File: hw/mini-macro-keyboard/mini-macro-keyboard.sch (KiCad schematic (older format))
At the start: 17 parts

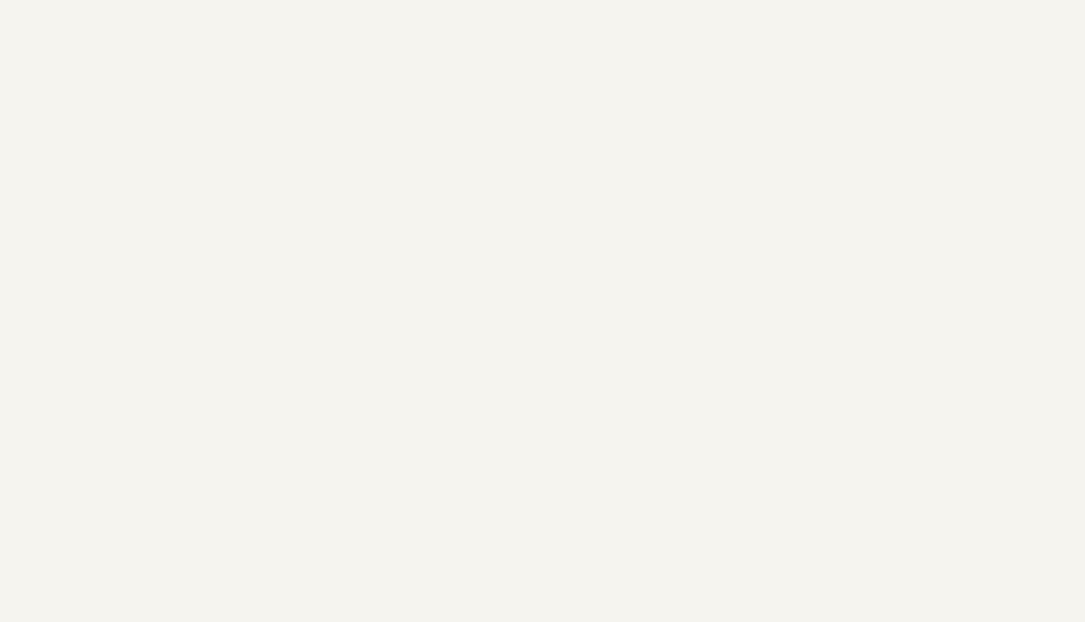
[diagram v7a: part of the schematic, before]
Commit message: feat(hw): add buck dc/dc converter to the schematic
Signed-off-by: Ivan Kovalenko <s1ckretbox@gmail.com>
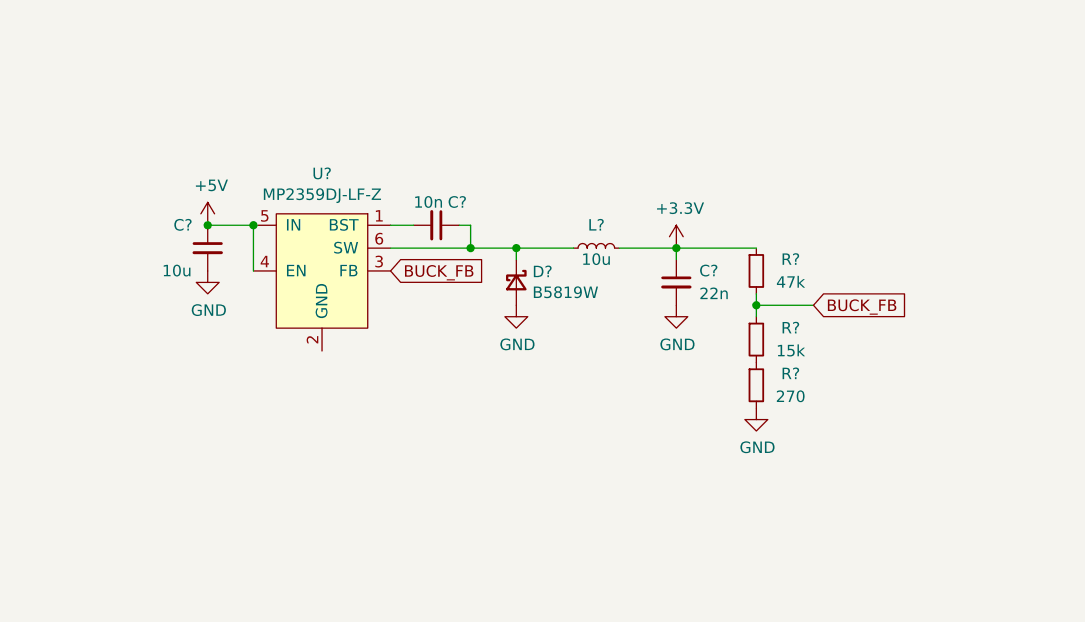
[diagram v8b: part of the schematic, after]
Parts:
- added C?: 10u, symbol Device:C_Small
- added C?: 10n, symbol Device:C_Small
- added C?: 22n, symbol Device:C_Small
- added D?: B5819W, symbol Device:D_Schottky_Small
- added L?: 10u, symbol Device:L_Small
- added R?: 47k, symbol Device:R_Small
- added R?: 15k, symbol Device:R_Small
- added R?: 270, symbol Device:R_Small
- added U?: MP2359DJ-LF-Z, symbol mini-macro-keyboard:MP2359DJ-LF-Z
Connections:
- net +3V3: now also C?.1, L?.2, R?.1
- net +5V: now also C?.1, U?.4 (EN), U?.5 (IN)
- net GND: now also C?.2, C?.2, D?.2 (A), R?.2
- new net: C?.2, U?.1 (BST)
- new net: C?.1, D?.1 (K), L?.1, U?.6 (SW)
- new net: R?.1, R?.2
- new net BUCK_FB: R?.1, R?.2, U?.3 (FB)
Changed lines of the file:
@@
 Text GLabel 7500 1100 2    50   Input ~ 0
 USB_D-
+$Comp
+L mini-macro-keyboard:MP2359DJ-LF-Z U?
+U 1 1 6003F08A
+P 4000 3000
+F 0 "U?" H 4000 3375 50  0000 C CNN
+F 1 "MP2359DJ-LF-Z" H 4000 3284 50  0000 C CNN
+F 2 "" H 4000 3000 50  0001 C CNN
+F 3 "" H 4000 3000 50  0001 C CNN
+	1    4000 3000
+	1    0    0    -1
+$EndComp
+$Comp
+L power:+5V #PWR?
+U 1 1 6003FF31
+P 3500 2850
+F 0 "#PWR?" H 3500 2700 50  0001 C CNN
+F 1 "+5V" H 3515 3023 50  0000 C CNN
+F 2 "" H 3500 2850 50  0001 C CNN
+F 3 "" H 3500 2850 50  0001 C CNN
+	1    3500 2850
+	1    0    0    -1
+$EndComp
+$Comp
+L power:GND #PWR?
+U 1 1 60040921
+P 3500 3050
+F 0 "#PWR?" H 3500 2800 50  0001 C CNN
+F 1 "GND" H 3505 2877 50  0000 C CNN
+F 2 "" H 3500 3050 50  0001 C CNN
+F 3 "" H 3500 3050 50  0001 C CNN
+	1    3500 3050
+	1    0    0    -1
+$EndComp
+$Comp
+L Device:C_Small C?
+U 1 1 600410FF
+P 3500 2950
+F 0 "C?" H 3350 3050 50  0000 L CNN
+F 1 "10u" H 3300 2850 50  0000 L CNN
+F 2 "" H 3500 2950 50  0001 C CNN
+F 3 "~" H 3500 2950 50  0001 C CNN
+	1    3500 2950
+	1    0    0    -1
+$EndComp
+Wire Wire Line
+	3700 2850 3700 3050
+Wire Wire Line
+	3700 2850 3500 2850
+Connection ~ 3700 2850
+Connection ~ 3500 2850
+$Comp
+L Device:D_Schottky_Small D?
+U 1 1 600485AC
+P 4850 3100
+F 0 "D?" V 4804 3170 50  0000 L CNN
+F 1 "B5819W" V 4895 3170 50  0000 L CNN
+F 2 "" V 4850 3100 50  0001 C CNN
+F 3 "~" V 4850 3100 50  0001 C CNN
+	1    4850 3100
+	0    1    1    0
+$EndComp
+$Comp
+L Device:C_Small C?
+U 1 1 600491AA
+P 4500 2850
+F 0 "C?" V 4400 2900 50  0000 L CNN
+F 1 "10n" V 4400 2750 50  0000 L CNN
+F 2 "" H 4500 2850 50  0001 C CNN
+F 3 "~" H 4500 2850 50  0001 C CNN
+	1    4500 2850
+	0    1    1    0
+$EndComp
+Wire Wire Line
+	4300 2850 4400 2850
+$Comp
+L Device:L_Small L?
+U 1 1 6004E9B3
+P 5200 2950
+F 0 "L?" V 5300 2950 50  0000 C CNN
+F 1 "10u" V 5150 2950 50  0000 C CNN
+F 2 "" H 5200 2950 50  0001 C CNN
+F 3 "~" H 5200 2950 50  0001 C CNN
+	1    5200 2950
+	0    -1   -1   0
+$EndComp
+$Comp
+L Device:C_Small C?
+U 1 1 600536F1
+P 5550 3100
+F 0 "C?" H 5650 3150 50  0000 L CNN
+F 1 "22n" H 5650 3050 50  0000 L CNN
+F 2 "" H 5550 3100 50  0001 C CNN
+F 3 "~" H 5550 3100 50  0001 C CNN
+	1    5550 3100
+	1    0    0    -1
+$EndComp
+$Comp
+L power:+3.3V #PWR?
+U 1 1 60055E76
+P 5550 2950
+F 0 "#PWR?" H 5550 2800 50  0001 C CNN
+F 1 "+3.3V" H 5565 3123 50  0000 C CNN
+F 2 "" H 5550 2950 50  0001 C CNN
+F 3 "" H 5550 2950 50  0001 C CNN
+	1    5550 2950
+	1    0    0    -1
+$EndComp
+Connection ~ 4850 2950
+Wire Wire Line
+	4850 2950 5100 2950
+Connection ~ 5550 2950
+Wire Wire Line
+	5300 2950 5550 2950
+$Comp
+L Device:R_Small R?
+U 1 1 600629FA
+P 5900 3050
+F 0 "R?" H 6050 3100 50  0000 C CNN
+F 1 "47k" H 6050 3000 50  0000 C CNN
+F 2 "" H 5900 3050 50  0001 C CNN
+F 3 "~" H 5900 3050 50  0001 C CNN
+	1    5900 3050
+	1    0    0    -1
+$EndComp
+$Comp
+L Device:R_Small R?
+U 1 1 60063979
+P 5900 3350
+F 0 "R?" H 6050 3400 50  0000 C CNN
+F 1 "15k" H 6050 3300 50  0000 C CNN
+F 2 "" H 5900 3350 50  0001 C CNN
+F 3 "~" H 5900 3350 50  0001 C CNN
+	1    5900 3350
+	1    0    0    -1
+$EndComp
+$Comp
+L Device:R_Small R?
+U 1 1 60063B85
+P 5900 3550
+F 0 "R?" H 6050 3600 50  0000 C CNN
+F 1 "270" H 6050 3500 50  0000 C CNN
+F 2 "" H 5900 3550 50  0001 C CNN
+F 3 "~" H 5900 3550 50  0001 C CNN
+	1    5900 3550
+	1    0    0    -1
+$EndComp
+$Comp
+L power:GND #PWR?
+U 1 1 600659EC
+P 5550 3200
+F 0 "#PWR?" H 5550 2950 50  0001 C CNN
+F 1 "GND" H 5555 3027 50  0000 C CNN
+F 2 "" H 5550 3200 50  0001 C CNN
+F 3 "" H 5550 3200 50  0001 C CNN
+	1    5550 3200
+	1    0    0    -1
+$EndComp
+Wire Wire Line
+	4850 2950 4850 3000
+$Comp
+L power:GND #PWR?
+U 1 1 6006E9D4
+P 4850 3200
+F 0 "#PWR?" H 4850 2950 50  0001 C CNN
+F 1 "GND" H 4855 3027 50  0000 C CNN
+F 2 "" H 4850 3200 50  0001 C CNN
+F 3 "" H 4850 3200 50  0001 C CNN
+	1    4850 3200
+	1    0    0    -1
+$EndComp
+Wire Wire Line
+	5550 2950 5550 3000
+$Comp
+L power:GND #PWR?
+U 1 1 6007A36C
+P 5900 3650
+F 0 "#PWR?" H 5900 3400 50  0001 C CNN
+F 1 "GND" H 5905 3477 50  0000 C CNN
+F 2 "" H 5900 3650 50  0001 C CNN
+F 3 "" H 5900 3650 50  0001 C CNN
+	1    5900 3650
+	1    0    0    -1
+$EndComp
+Wire Wire Line
+	5900 2950 5550 2950
+Text GLabel 4300 3050 2    50   Input ~ 0
+BUCK_FB
+Text GLabel 6150 3200 2    50   Input ~ 0
+BUCK_FB
+Wire Wire Line
+	5900 3150 5900 3200
+Wire Wire Line
+	6150 3200 5900 3200
+Connection ~ 5900 3200
+Wire Wire Line
+	5900 3200 5900 3250
+Wire Wire Line
+	4300 2950 4650 2950
+Wire Wire Line
+	4600 2850 4650 2850
+Wire Wire Line
+	4650 2850 4650 2950
+Connection ~ 4650 2950
+Wire Wire Line
+	4650 2950 4850 2950
 $EndSCHEMATC
